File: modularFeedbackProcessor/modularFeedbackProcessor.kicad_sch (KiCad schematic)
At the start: 76 parts, among them J1 Input, J10 Double, J11 Feedback, J12 EffectsDryWet, J2 DryWet, J3 Output, J4 EffectRouteOut, J5 EffectRouteIn, J6 Rate, J9 Inhibit, Q1 NJFET, Q6 Q_PMOS_GDS, U1 V3205, U10 TL074, U2 CD4046, U4 RC4558, U6 TL074, U7 LM13700, U8 LF398_DIP8, U9 TL074

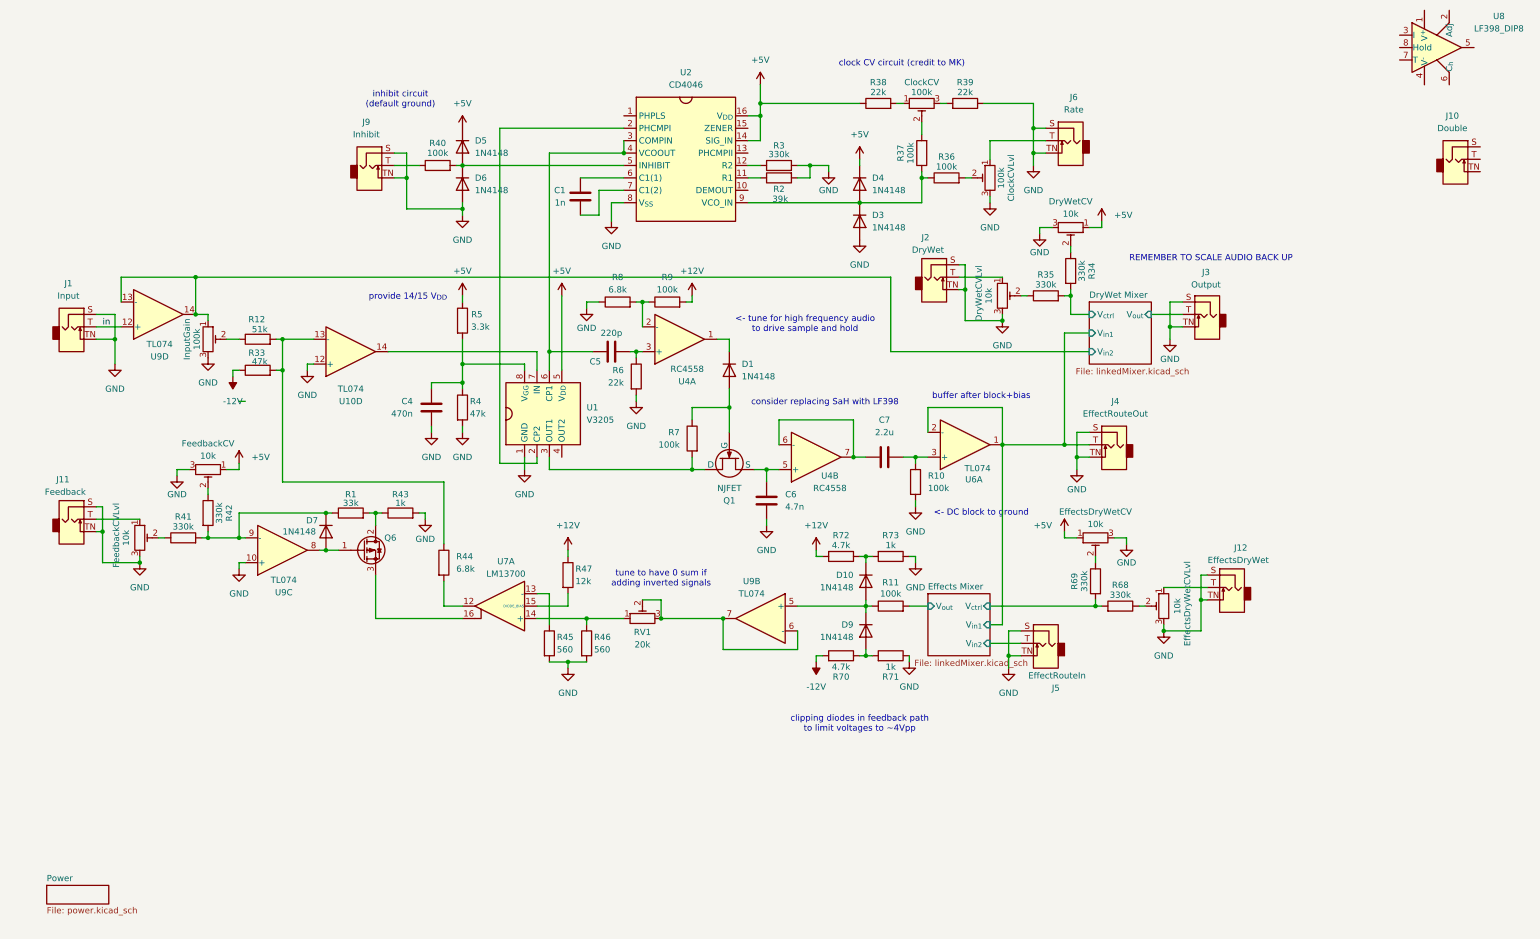
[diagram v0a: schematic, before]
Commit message: more fixes, touch ups. implemented rescaling of the output.
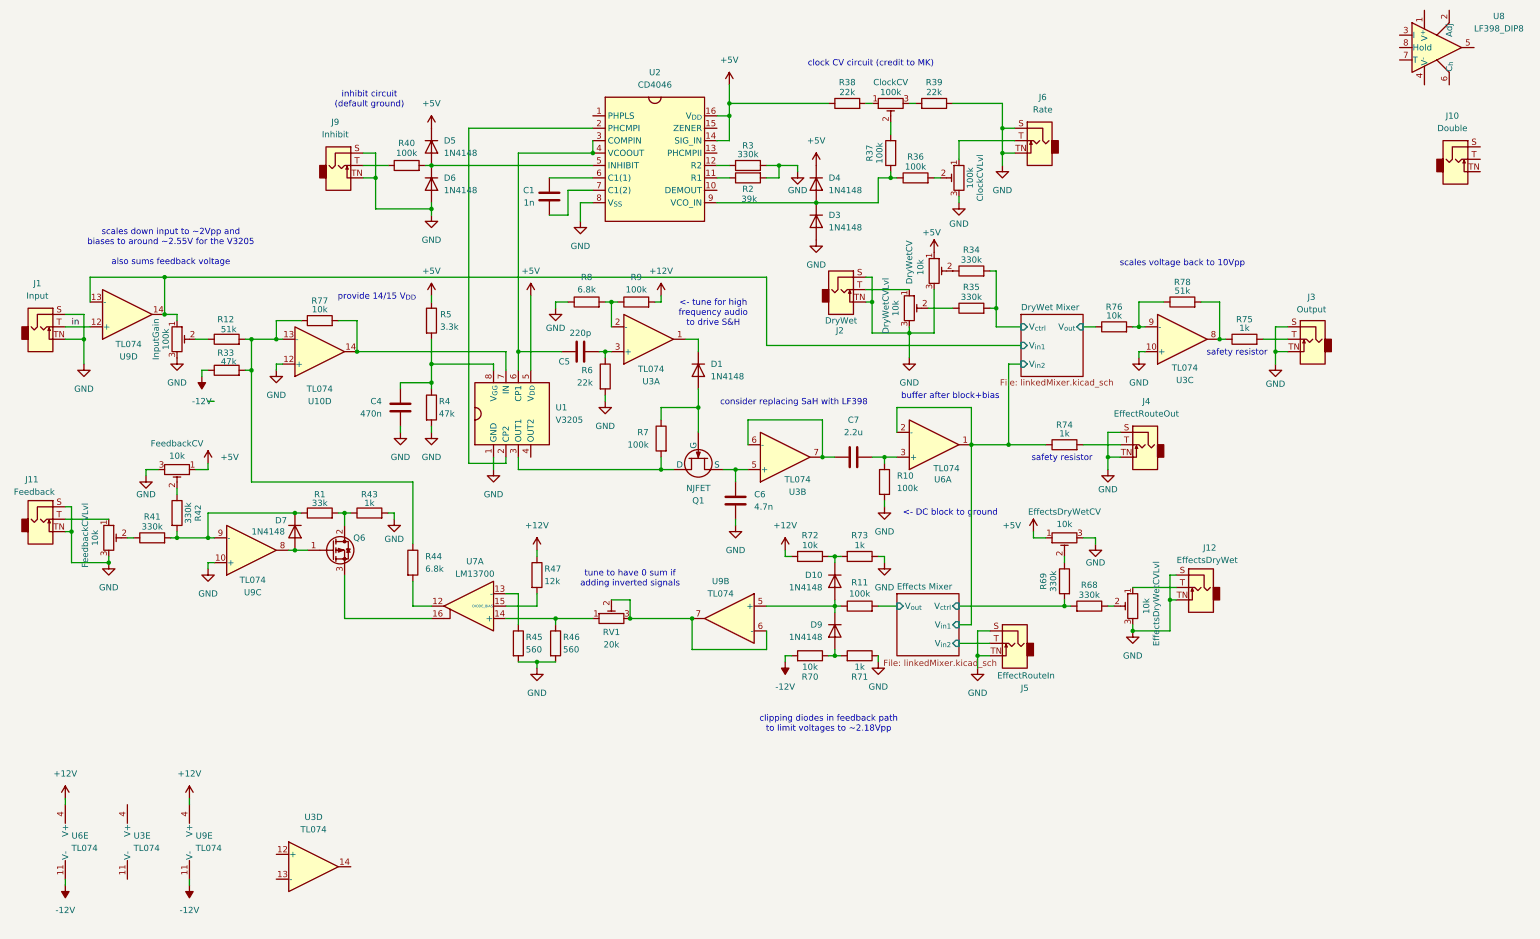
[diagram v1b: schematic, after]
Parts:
- removed U4: RC4558, symbol Amplifier_Operational:RC4558
- added R74, R75: 1k, symbol Device:R
- added R76, R77: 10k, symbol Device:R
- added R78: 51k, symbol Device:R
- added U3: TL074, symbol Amplifier_Operational:TL074
- added unit 5 of U6
- added unit 5 of U9
- R70, R72: value 4.7k -> 10k
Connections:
- net +12V: now also U6.4 (V+), U9.4 (V+)
- net -12V: now also U6.11 (V-), U9.11 (V-)
- net DryWet Mixer/V_{in1}: now also InputGain.1, U9.13 (-), U9.14; no longer J4.T, U6.1, U6.2 (-)
- net DryWet Mixer/V_{in2}: now also U6.1, U6.2 (-), R74.1; no longer InputGain.1, U9.13 (-), U9.14
- net DryWet Mixer/V_{out}: now also R76.1; no longer J3.T
- net GND: now also U3.10 (+)
- net at C7.2: now also U3.6 (-), U3.7
- net at C6.1, Q1.3 (S): now also U3.5 (+)
- net at R12.2, R33.2, R44.1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: now also R77.1
- net at U1.7 (IN), U10.14: now also R77.2
- net at C5.2, R6.1: now also U3.3 (+)
- net at D1.1 (K): now also U3.1
- net at R8.2, R9.1: now also U3.2 (-)
- new net: J4.T, R74.2
- new net: R75.1, R78.2, U3.8
- new net: J3.T, R75.2
- new net: R76.2, R78.1, U3.9 (-)
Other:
- removed sheet Power
- note added: "<- tune for high frequency audio to drive S&H"
- note added: "clipping diodes in feedback path to limit voltages to ~2.18Vpp"
- note added: "safety resistor"
- note added: "scales down input to ~2Vpp and biases to around ~2.55V for the V3205 also sums feedback voltage"
- note added: "scales voltage back to 10Vpp"
- note removed: "<- tune for high frequency audio to drive sample and hold"
- note removed: "REMEMBER TO SCALE AUDIO BACK UP"
- note removed: "clipping diodes in feedback path to limit voltages to ~4Vpp"
- moved on the sheet: C1, C4, C5, C6, C7, ClockCV, ClockCVLvl, D1, D10, D3, D4, D5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

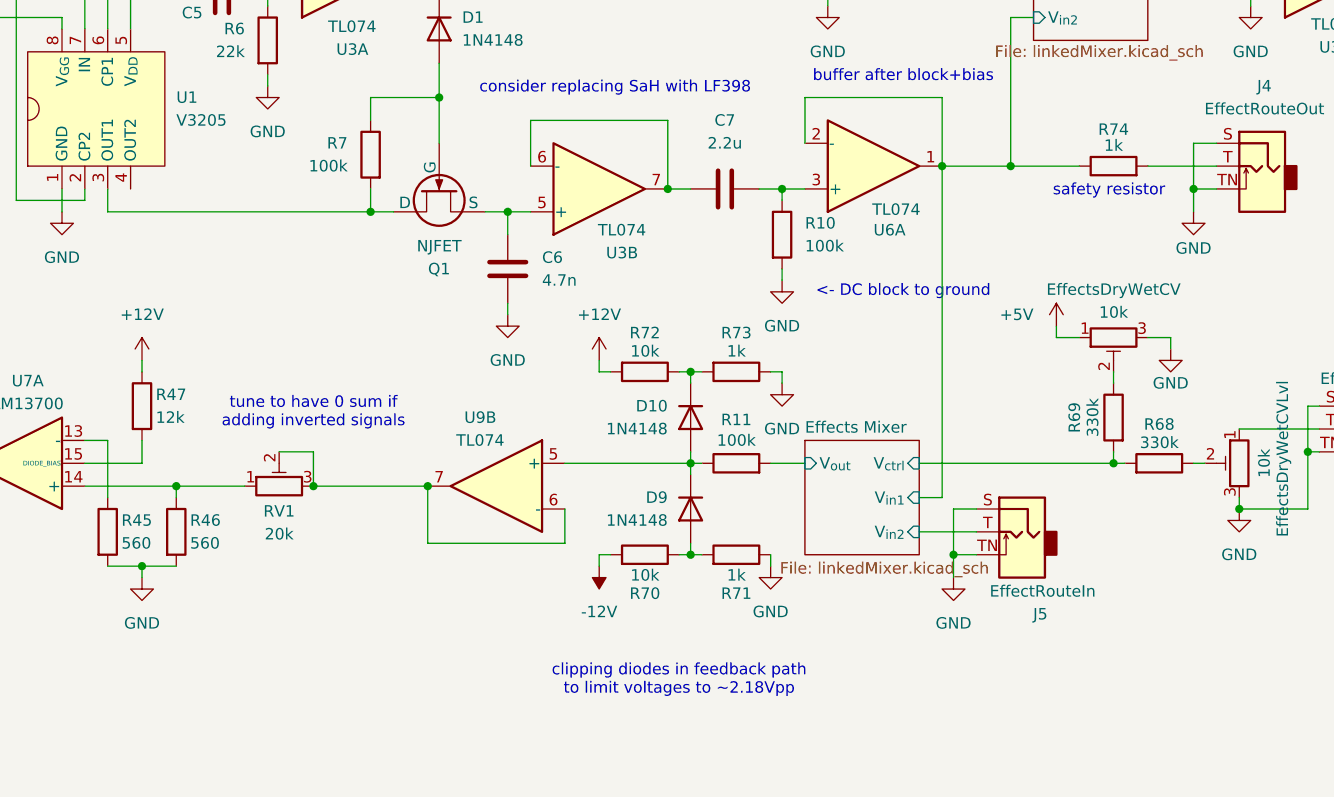
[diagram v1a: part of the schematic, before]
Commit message: added switch to turn on/off effect routing
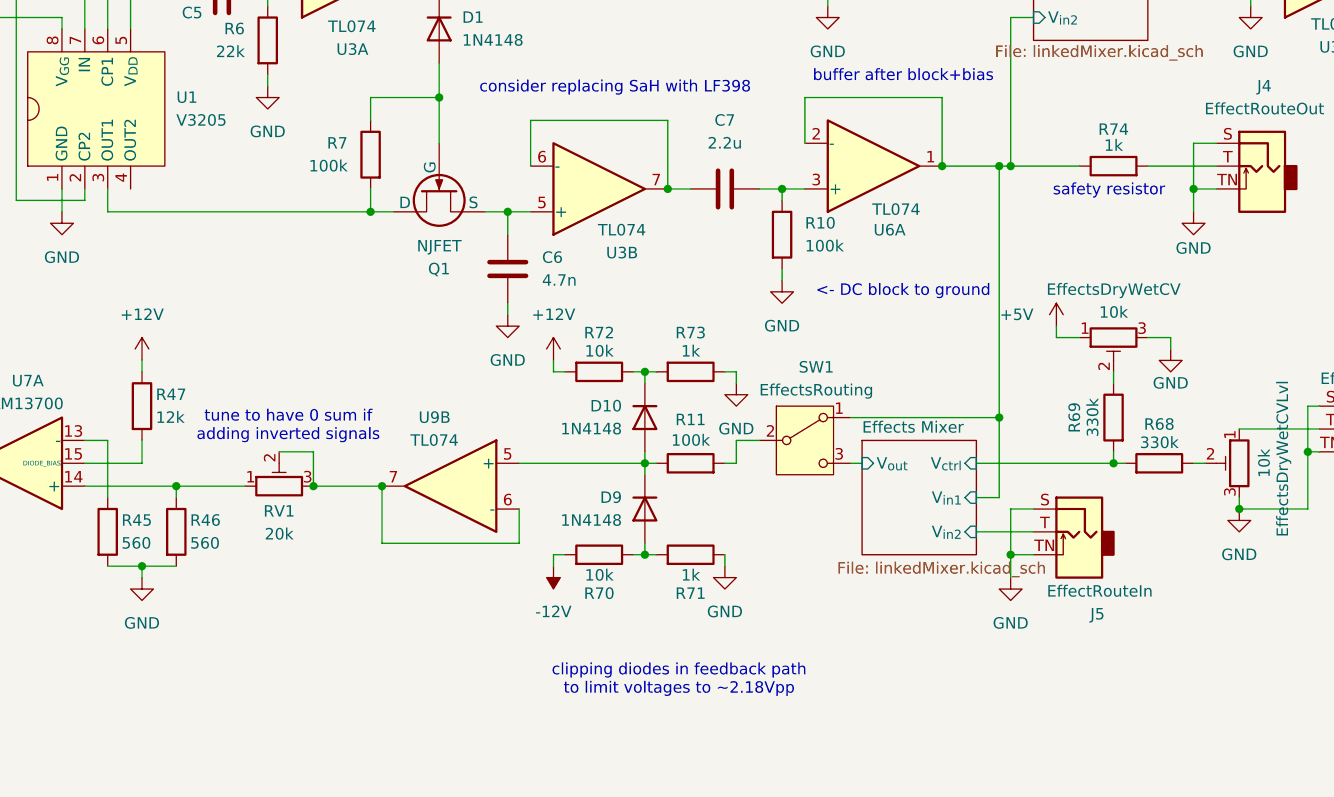
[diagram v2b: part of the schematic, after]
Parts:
- added SW1: EffectsRouting, symbol Switch:SW_SPDT
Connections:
- net DryWet Mixer/V_{in2}: now also SW1.1 (A)
- net Effects Mixer/V_{out}: now also SW1.3 (C); no longer R11.2
- new net: R11.2, SW1.2 (B)
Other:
- moved on the sheet: D10, D9, J5, R11, R70, R71, R72, R73, U9B

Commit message: pushing changes
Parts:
- C1: renamed from C4; footprint (none) -> Capacitor_THT:C_Disc_D4.7mm_W2.5mm_P5.00mm
- C2: renamed from C1; footprint (none) -> Capacitor_THT:C_Disc_D4.7mm_W2.5mm_P5.00mm
- C3: renamed from C5; footprint (none) -> Capacitor_THT:C_Disc_D4.7mm_W2.5mm_P5.00mm
- C4: renamed from C6; footprint (none) -> Capacitor_THT:C_Disc_D4.7mm_W2.5mm_P5.00mm
- C5: renamed from C7; footprint (none) -> Capacitor_THT:CP_Radial_D5.0mm_P2.50mm
- renumbered ClockCV to ClockCV1, ClockCVLvl to ClockCVLvl1, D7 to D1, D5 to D2, D6 to D3, D1 to D4, D10 to D5, D9 to D6, D4 to D7, D3 to D8, DryWetCV to DryWetCV1, DryWetCVLvl to DryWetCVLvl1, EffectsDryWetCV to EffectsDryWetCV1, EffectsDryWetCVLvl to EffectsDryWetCVLvl1, FeedbackCV to FeedbackCV1, FeedbackCVLvl to FeedbackCVLvl1, InputGain to InputGain1, J11 to J2, J9 to J3, J2 to J4, J6 to J5, J5 to J6, J4 to J7, J12 to J8, J3 to J9, Q6 to Q1, Q1 to Q2, R41 to R1, R5 to R10, R4 to R11, R45 to R12, R47 to R13, R46 to R14, R8 to R15, R6 to R16, R9 to R17, R7 to R18, R3 to R19, R42 to R2, R2 to R20, R72 to R21, R70 to R22, R73 to R23, R11 to R24, R71 to R25, R38 to R26, R10 to R27, R37 to R28, R36 to R29, R12 to R3, R39 to R30, R34 to R31, R35 to R32, R74 to R33, R69 to R34, R68 to R35, R76 to R36, R78 to R37, R75 to R38, R33 to R4, R77 to R5, R1 to R6, R43 to R7, R40 to R8, R44 to R9, U6 to U1, U9 to U2, U10 to U4, U7 to U5, U1 to U6, U2 to U7
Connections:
- net +12V: now also U3.4 (V+)
- net -12V: now also U3.11 (V-)

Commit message: fixed 6.8k resistor location in feedback VCA
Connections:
- net at U5.12: now also R3.2, R4.2, R5.1, U4.13 (-); no longer R9.2
- net at U5.16: now also R9.1; no longer Q1.3 (S)
- new net: Q1.3 (S), R9.2
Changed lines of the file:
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@@
 	(wire
 		(pts
-			(xy 95.25 124.46) (xy 95.25 129.54)
-		)
-		(stroke
-			(width 0)
-			(type default)
-		)
-	)
-	(wire
-		(pts
 			(xy 151.13 74.93) (xy 153.67 74.93)
 		)
@@
 	(wire
 		(pts
+			(xy 81.28 132.08) (xy 85.09 132.08)
+		)
+		(stroke
+			(width 0)
+			(type default)
+		)
+	)
+	(wire
+		(pts
 			(xy 116.84 36.83) (xy 132.08 36.83)
 		)
@@
 	(wire
 		(pts
+			(xy 92.71 132.08) (xy 99.06 132.08)
+		)
+		(stroke
+			(width 0)
+			(type default)
+		)
+	)
+	(wire
+		(pts
 			(xy 179.07 91.44) (xy 179.07 99.06)
 		)
@@
 	(wire
 		(pts
-			(xy 81.28 132.08) (xy 99.06 132.08)
-		)
-		(stroke
-			(width 0)
-			(type default)
-		)
-	)
-	(wire
-		(pts
 			(xy 46.99 115.57) (xy 53.34 115.57)
 		)
@@
 	(wire
 		(pts
-			(xy 95.25 104.14) (xy 95.25 116.84)
+			(xy 95.25 104.14) (xy 95.25 129.54)
 		)
 		(stroke
@@
 	(symbol
 		(lib_id "Device:R")
+		(at 88.9 132.08 270)
+		(unit 1)
+		(body_style 1)
+		(exclude_from_sim no)
+		(in_bom yes)
+		(on_board yes)
+		(in_pos_files yes)
+		(dnp no)
+		(property "Reference" "R9"
+			(at 88.9 128.016 90)
+			(show_name no)
+			(do_not_autoplace no)
+			(effects
+				(font
+					(size 1.27 1.27)
+				)
+			)
+		)
+		(property "Value" "6.8k"
+			(at 88.9 129.794 90)
+			(show_name no)
+			(do_not_autoplace no)
+			(effects
+				(font
+					(size 1.27 1.27)
+				)
+			)
+		)
+		(property "Footprint" ""
+			(at 88.9 130.302 90)
+			(hide yes)
+			(show_name no)
+			(do_not_autoplace no)
+			(effects
+				(font
+					(size 1.27 1.27)
+				)
+			)
+		)
+		(property "Datasheet" ""
+			(at 88.9 132.08 0)
+			(hide yes)
+			(show_name no)
+			(do_not_autoplace no)
+			(effects
+				(font
+					(size 1.27 1.27)
+				)
+			)
+		)
+		(property "Description" "Resistor"
+			(at 88.9 132.08 0)
+			(hide yes)
+			(show_name no)
+			(do_not_autoplace no)
+			(effects
+				(font
+					(size 1.27 1.27)
+				)
+			)
+		)
+		(pin "2"
+		)
+		(pin "1"
+		)
+		(instances
+			(project "modularFeedbackProcessor"
+				(path "/a81d404d-f7d3-4fe2-a135-d74fc6d7b6a7"
+					(reference "R9")
+					(unit 1)
+				)
+			)
+		)
+	)
+	(symbol
+		(lib_id "Device:R")
 		(at 46.99 110.49 0)
 		(unit 1)
@@
 					)
 				)
-			)
-		)
-	)
-	(symbol
-		(lib_id "Device:R")
-		(at 95.25 120.65 0)
-		(unit 1)
-		(body_style 1)
-		(exclude_from_sim no)
-		(in_bom yes)
-		(on_board yes)
-		(in_pos_files yes)
-		(dnp no)
-		(fields_autoplaced yes)
-		(property "Reference" "R9"
-			(at 97.79 119.3799 0)
-			(show_name no)
-			(do_not_autoplace no)
-			(effects
-				(font
-					(size 1.27 1.27)
-				)
-				(justify left)
-			)
-		)
-		(property "Value" "6.8k"
-			(at 97.79 121.9199 0)
-			(show_name no)
-			(do_not_autoplace no)
-			(effects
-				(font
-					(size 1.27 1.27)
-				)
-				(justify left)
-			)
-		)
-		(property "Footprint" ""
-			(at 93.472 120.65 90)
-			(hide yes)
-			(show_name no)
-			(do_not_autoplace no)
-			(effects
-				(font
-					(size 1.27 1.27)
-				)
-			)
-		)
-		(property "Datasheet" ""
-			(at 95.25 120.65 0)
-			(hide yes)
-			(show_name no)
-			(do_not_autoplace no)
-			(effects
-				(font
-					(size 1.27 1.27)
-				)
-			)
-		)
-		(property "Description" "Resistor"
-			(at 95.25 120.65 0)
-			(hide yes)
-			(show_name no)
-			(do_not_autoplace no)
-			(effects
-				(font
-					(size 1.27 1.27)
-				)
-			)
-		)
-		(pin "2"
-		)
-		(pin "1"
-		)
-		(instances
-			(project "modularFeedbackProcessor"
-				(path "/a81d404d-f7d3-4fe2-a135-d74fc6d7b6a7"
-					(reference "R9")
-					(unit 1)
-					(variant
-						(name "Testing")
-						(field
-							(name "Footprint")
-							(value "Resistor_THT:R_Axial_DIN0309_L9.0mm_D3.2mm_P12.70mm_Horizontal")
-						)
-					)
-				)

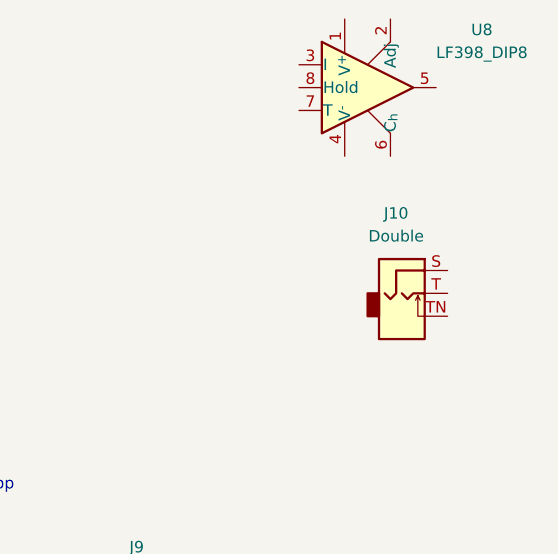
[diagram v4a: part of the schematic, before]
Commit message: last commit before attempting to change the S&H to the LF398
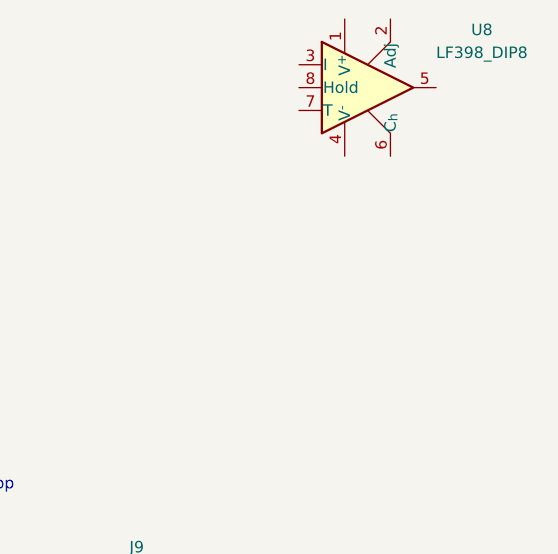
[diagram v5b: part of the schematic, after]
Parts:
- removed J10: Double, symbol Connector_Audio:AudioJack2_SwitchT
- J1, J2, J3, J4, J5, J6, J7, J8, J9: footprint (none) -> PCM_Eurocad:PJ301M-12
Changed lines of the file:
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@@
 			)
 		)
-		(property "Footprint" ""
+		(property "Footprint" "PCM_Eurocad:PJ301M-12"
 			(at 223.52 34.29 0)
 			(hide yes)
@@
 			)
 		)
-		(property "Footprint" ""
+		(property "Footprint" "PCM_Eurocad:PJ301M-12"
 			(at 256.54 125.73 0)
 			(hide yes)
@@
 			)
 		)
-		(property "Footprint" ""
+		(property "Footprint" "PCM_Eurocad:PJ301M-12"
 			(at 19.05 111.76 0)
 			(hide yes)
@@
 			)
 		)
-		(property "Footprint" ""
+		(property "Footprint" "PCM_Eurocad:PJ301M-12"
 			(at 80.01 39.37 0)
 			(hide yes)
@@
 			)
 		)
-		(property "Footprint" ""
+		(property "Footprint" "PCM_Eurocad:PJ301M-12"
 			(at 182.88 64.77 0)
 			(hide yes)
@@
 			)
 		)
-		(property "Footprint" ""
+		(property "Footprint" "PCM_Eurocad:PJ301M-12"
 			(at 224.79 137.16 0)
 			(hide yes)
@@
 	)
 	(symbol
-		(lib_id "Connector_Audio:AudioJack2_SwitchT")
-		(at 308.61 38.1 0)
-		(unit 1)
-		(body_style 1)
-		(exclude_from_sim no)
-		(in_bom yes)
-		(on_board yes)
-		(in_pos_files yes)
-		(dnp no)
-		(fields_autoplaced yes)
-		(property "Reference" "J10"
-			(at 307.975 29.21 0)
-			(show_name no)
-			(do_not_autoplace no)
-			(effects
-				(font
-					(size 1.27 1.27)
-				)
-			)
-		)
-		(property "Value" "Double"
-			(at 307.975 31.75 0)
-			(show_name no)
-			(do_not_autoplace no)
-			(effects
-				(font
-					(size 1.27 1.27)
-				)
-			)
-		)
-		(property "Footprint" ""
-			(at 308.61 38.1 0)
-			(hide yes)
-			(show_name no)
-			(do_not_autoplace no)
-			(effects
-				(font
-					(size 1.27 1.27)
-				)
-			)
-		)
-		(property "Datasheet" ""
-			(at 308.61 38.1 0)
-			(hide yes)
-			(show_name no)
-			(do_not_autoplace no)
-			(effects
-				(font
-					(size 1.27 1.27)
-				)
-			)
-		)
-		(property "Description" "Audio Jack, 2 Poles (Mono / TS), Switched T Pole (Normalling)"
-			(at 308.61 38.1 0)
-			(hide yes)
-			(show_name no)
-			(do_not_autoplace no)
-			(effects
-				(font
-					(size 1.27 1.27)
-				)
-			)
-		)
-		(pin "T"
-		)
-		(pin "S"
-		)
-		(pin "TN"
-		)
-		(instances
-			(project "modularFeedbackProcessor"
-				(path "/a81d404d-f7d3-4fe2-a135-d74fc6d7b6a7"
-					(reference "J10")
-					(unit 1)
-					(variant
-						(name "Testing")
-					)
-				)
-			)
-		)
-	)
-	(symbol
 		(lib_id "power:+5V")
 		(at 222.25 114.3 0)
@@
 			)
 		)
-		(property "Footprint" ""
+		(property "Footprint" "PCM_Eurocad:PJ301M-12"
 			(at 19.05 72.39 0)
 			(hide yes)
@@
 			)
 		)
-		(property "Footprint" ""
+		(property "Footprint" "PCM_Eurocad:PJ301M-12"
 			(at 279.4 74.93 0)
 			(hide yes)
@@
 			)
 		)
-		(property "Footprint" ""
+		(property "Footprint" "PCM_Eurocad:PJ301M-12"
 			(at 245.11 96.52 0)
 			(hide yes)
